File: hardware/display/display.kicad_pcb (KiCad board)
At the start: 2 copper layers, 110 x 70 mm, 7 parts, among them J1 Conn_02x03_Odd_Even

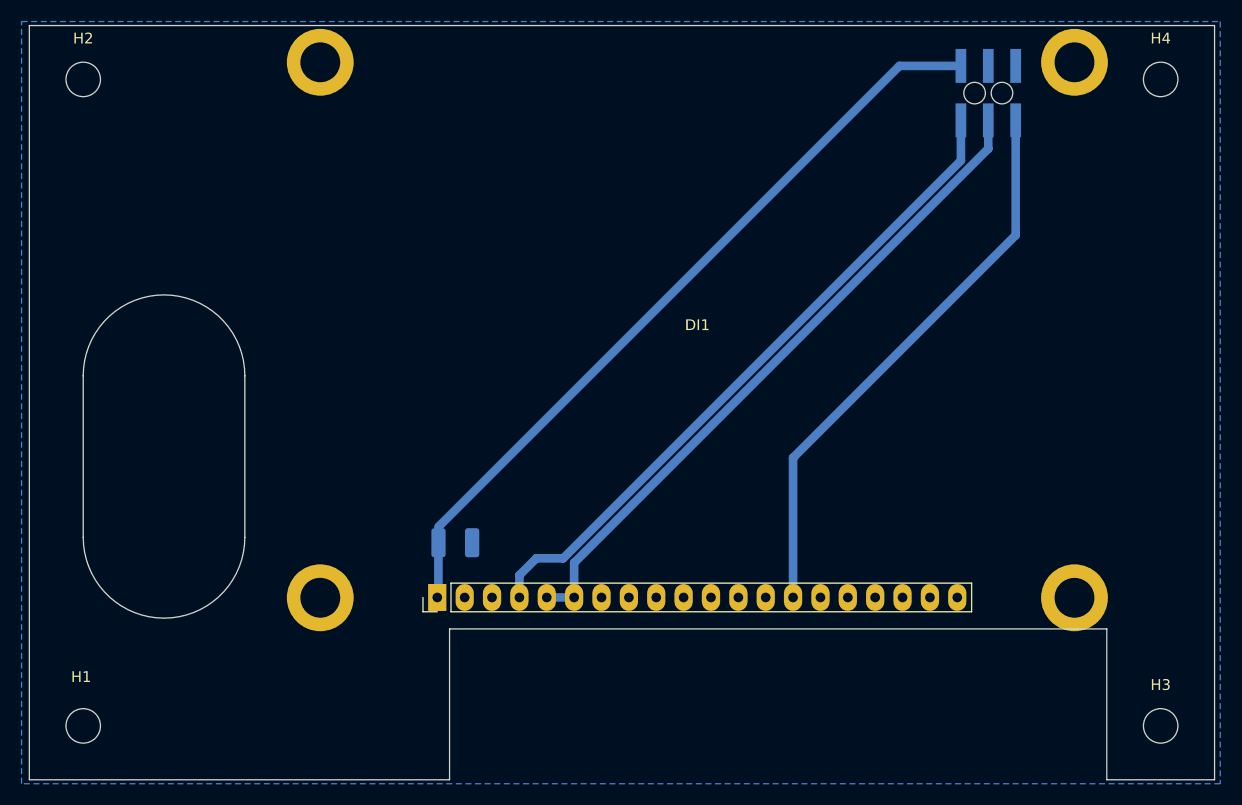
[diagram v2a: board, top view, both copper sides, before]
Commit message: Connect mounting holes to GND
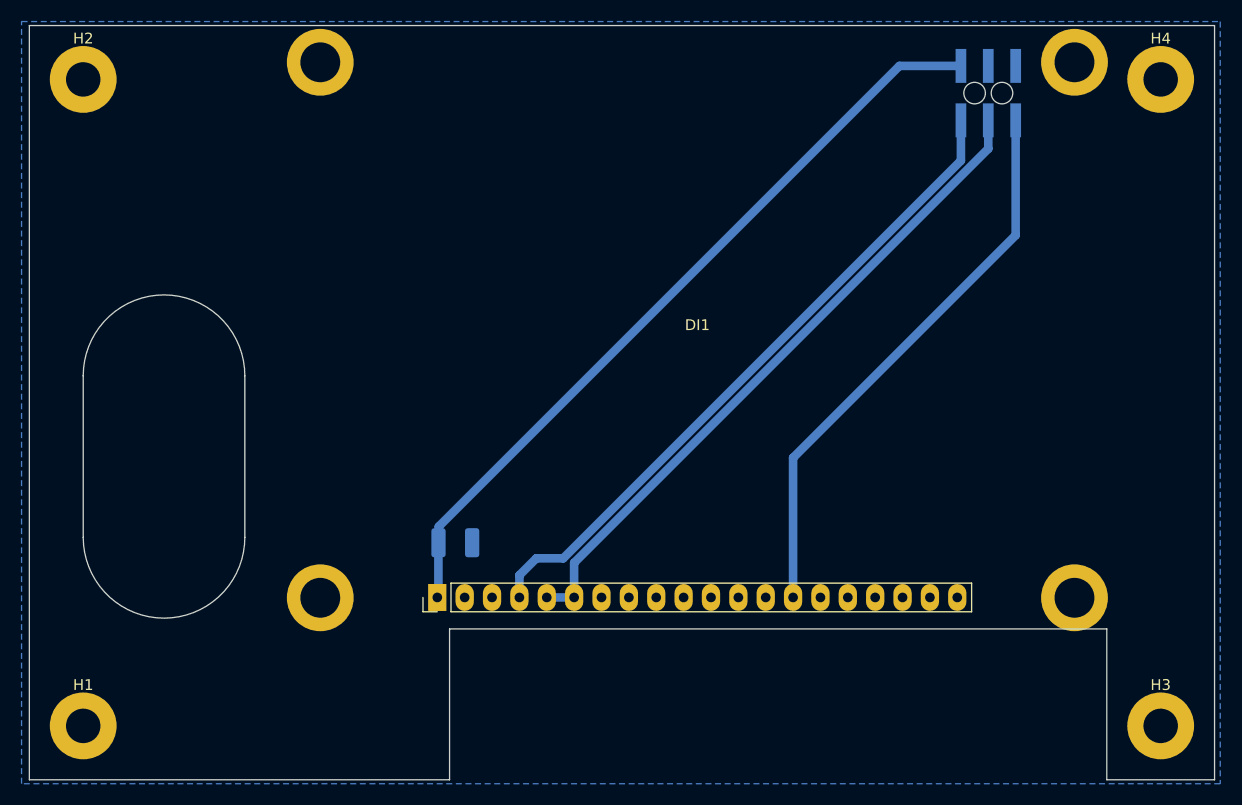
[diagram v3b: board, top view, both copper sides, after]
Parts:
- H1: footprint MountingHole:MountingHole_3.2mm_M3_DIN965 -> MountingHole:MountingHole_3.2mm_M3_DIN965_Pad
- H2, H3, H4: value 3.2mm -> MountingHole_Pad; footprint MountingHole:MountingHole_3.2mm_M3_DIN965 -> MountingHole:MountingHole_3.2mm_M3_DIN965_Pad
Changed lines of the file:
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@@
   (net 10 "/~{RST_DISP}")
   (net 11 "unconnected-(J1-Pad2)")
-  (footprint "MountingHole:MountingHole_3.2mm_M3_DIN965" locked (layer "F.Cu")
+  (footprint "MountingHole:MountingHole_3.2mm_M3_DIN965_Pad" locked (layer "F.Cu")
     (at 155 145)
-    (descr "Mounting Hole 3.2mm, no annular, M3, DIN965")
-    (tags "mounting hole 3.2mm no annular m3 din965")
+    (descr "Mounting Hole 3.2mm, M3, DIN965")
+    (tags "mounting hole 3.2mm m3 din965")
     (property "Sheetfile" "display.kicad_sch")
     (property "Sheetname" "")
@@
       (effects (font (size 1 1) (thickness 0.15)))
     )
-    (fp_text value "3.2mm" (at 0 3.8) (layer "F.Fab")
-      (effects (font (size 1 1) (thickness 0.15)))
-    )
-    (fp_text user "${REFERENCE}" (at 0 0) (layer "F.Fab")
-      (effects (font (size 1 1) (thickness 0.15)))
-    )
-    (fp_circle (center 0 0) (end 2.8 0) (layer "Cmts.User") (width 0.15) (fill none))
-    (fp_circle (center 0 0) (end 3.05 0) (layer "F.CrtYd") (width 0.05) (fill none))
-    (pad "" np_thru_hole circle locked (at 0 0) (size 3.2 3.2) (drill 3.2) (layers *.Cu *.Mask))
+    (fp_text value "MountingHole_Pad" (at 0 3.8) (layer "F.Fab")
+      (effects (font (size 1 1) (thickness 0.15)))
+    )
+    (fp_text user "${REFERENCE}" (at 0 0) (layer "F.Fab")
+      (effects (font (size 1 1) (thickness 0.15)))
+    )
+    (fp_circle (center 0 0) (end 2.8 0) (layer "Cmts.User") (width 0.15) (fill none))
+    (fp_circle (center 0 0) (end 3.05 0) (layer "F.CrtYd") (width 0.05) (fill none))
+    (pad "1" thru_hole circle locked (at 0 0) (size 6.2 6.2) (drill 3.2) (layers *.Cu *.Mask)
+      (net 1 "GND") (pinfunction "1") (pintype "input"))
   )
   (footprint "LCDdisplays.mod:MCOB128064JX" (layer "F.Cu")
@@
     )
   )
-  (footprint "MountingHole:MountingHole_3.2mm_M3_DIN965" locked (layer "F.Cu")
+  (footprint "MountingHole:MountingHole_3.2mm_M3_DIN965_Pad" locked (layer "F.Cu")
     (at 55 85)
-    (descr "Mounting Hole 3.2mm, no annular, M3, DIN965")
-    (tags "mounting hole 3.2mm no annular m3 din965")
+    (descr "Mounting Hole 3.2mm, M3, DIN965")
+    (tags "mounting hole 3.2mm m3 din965")
     (property "Sheetfile" "display.kicad_sch")
     (property "Sheetname" "")
@@
       (effects (font (size 1 1) (thickness 0.15)))
     )
+    (fp_text value "MountingHole_Pad" (at 0 3.8) (layer "F.Fab")
+      (effects (font (size 1 1) (thickness 0.15)))
+    )
+    (fp_text user "${REFERENCE}" (at 0 0) (layer "F.Fab")
+      (effects (font (size 1 1) (thickness 0.15)))
+    )
+    (fp_circle (center 0 0) (end 2.8 0) (layer "Cmts.User") (width 0.15) (fill none))
+    (fp_circle (center 0 0) (end 3.05 0) (layer "F.CrtYd") (width 0.05) (fill none))
+    (pad "1" thru_hole circle locked (at 0 0) (size 6.2 6.2) (drill 3.2) (layers *.Cu *.Mask)
+      (net 1 "GND") (pinfunction "1") (pintype "input"))
+  )
+  (footprint "MountingHole:MountingHole_3.2mm_M3_DIN965_Pad" locked (layer "F.Cu")
+    (at 55 145)
+    (descr "Mounting Hole 3.2mm, M3, DIN965")
+    (tags "mounting hole 3.2mm m3 din965")
+    (property "Sheetfile" "display.kicad_sch")
+    (property "Sheetname" "")
+    (attr exclude_from_pos_files)
+    (fp_text reference "H1" (at 0 -3.8) (layer "F.SilkS")
+      (effects (font (size 1 1) (thickness 0.15)))
+    )
     (fp_text value "3.2mm" (at 0 3.8) (layer "F.Fab")
       (effects (font (size 1 1) (thickness 0.15)))
@@
     (fp_circle (center 0 0) (end 2.8 0) (layer "Cmts.User") (width 0.15) (fill none))
     (fp_circle (center 0 0) (end 3.05 0) (layer "F.CrtYd") (width 0.05) (fill none))
-    (pad "" np_thru_hole circle locked (at 0 0) (size 3.2 3.2) (drill 3.2) (layers *.Cu *.Mask))
-  )
-  (footprint "MountingHole:MountingHole_3.2mm_M3_DIN965" locked (layer "F.Cu")
-    (at 55 145)
-    (descr "Mounting Hole 3.2mm, no annular, M3, DIN965")
-    (tags "mounting hole 3.2mm no annular m3 din965")
-    (property "Sheetfile" "display.kicad_sch")
-    (property "Sheetname" "")
-    (attr exclude_from_pos_files)
-    (fp_text reference "H1" (at -0.188 -4.538) (layer "F.SilkS")
-      (effects (font (size 1 1) (thickness 0.15)))
-    )
-    (fp_text value "3.2mm" (at 0 3.8) (layer "F.Fab")
-      (effects (font (size 1 1) (thickness 0.15)))
-    )
-    (fp_text user "${REFERENCE}" (at 0 0) (layer "F.Fab")
-      (effects (font (size 1 1) (thickness 0.15)))
-    )
-    (fp_circle (center 0 0) (end 2.8 0) (layer "Cmts.User") (width 0.15) (fill none))
-    (fp_circle (center 0 0) (end 3.05 0) (layer "F.CrtYd") (width 0.05) (fill none))
-    (pad "" np_thru_hole circle locked (at 0 0) (size 3.2 3.2) (drill 3.2) (layers *.Cu *.Mask))
-  )
-  (footprint "MountingHole:MountingHole_3.2mm_M3_DIN965" locked (layer "F.Cu")
+    (pad "1" thru_hole circle locked (at 0 0) (size 6.2 6.2) (drill 3.2) (layers *.Cu *.Mask)
+      (net 1 "GND") (pinfunction "1") (pintype "input"))
+  )
+  (footprint "MountingHole:MountingHole_3.2mm_M3_DIN965_Pad" locked (layer "F.Cu")
     (at 155 85)
-    (descr "Mounting Hole 3.2mm, no annular, M3, DIN965")
-    (tags "mounting hole 3.2mm no annular m3 din965")
+    (descr "Mounting Hole 3.2mm, M3, DIN965")
+    (tags "mounting hole 3.2mm m3 din965")
     (property "Sheetfile" "display.kicad_sch")
     (property "Sheetname" "")
@@
       (effects (font (size 1 1) (thickness 0.15)))
     )
-    (fp_text value "3.2mm" (at 0 3.8) (layer "F.Fab")
-      (effects (font (size 1 1) (thickness 0.15)))
-    )
-    (fp_text user "${REFERENCE}" (at 0 0) (layer "F.Fab")
-      (effects (font (size 1 1) (thickness 0.15)))
-    )
-    (fp_circle (center 0 0) (end 2.8 0) (layer "Cmts.User") (width 0.15) (fill none))
-    (fp_circle (center 0 0) (end 3.05 0) (layer "F.CrtYd") (width 0.05) (fill none))
-    (pad "" np_thru_hole circle locked (at 0 0) (size 3.2 3.2) (drill 3.2) (layers *.Cu *.Mask))
+    (fp_text value "MountingHole_Pad" (at 0 3.8) (layer "F.Fab")
+      (effects (font (size 1 1) (thickness 0.15)))
+    )
+    (fp_text user "${REFERENCE}" (at 0 0) (layer "F.Fab")
+      (effects (font (size 1 1) (thickness 0.15)))
+    )
+    (fp_circle (center 0 0) (end 2.8 0) (layer "Cmts.User") (width 0.15) (fill none))
+    (fp_circle (center 0 0) (end 3.05 0) (layer "F.CrtYd") (width 0.05) (fill none))
+    (pad "1" thru_hole circle locked (at 0 0) (size 6.2 6.2) (drill 3.2) (layers *.Cu *.Mask)
+      (net 1 "GND") (pinfunction "1") (pintype "input"))
   )
   (footprint "harwin:M20-8750342" locked (layer "B.Cu")

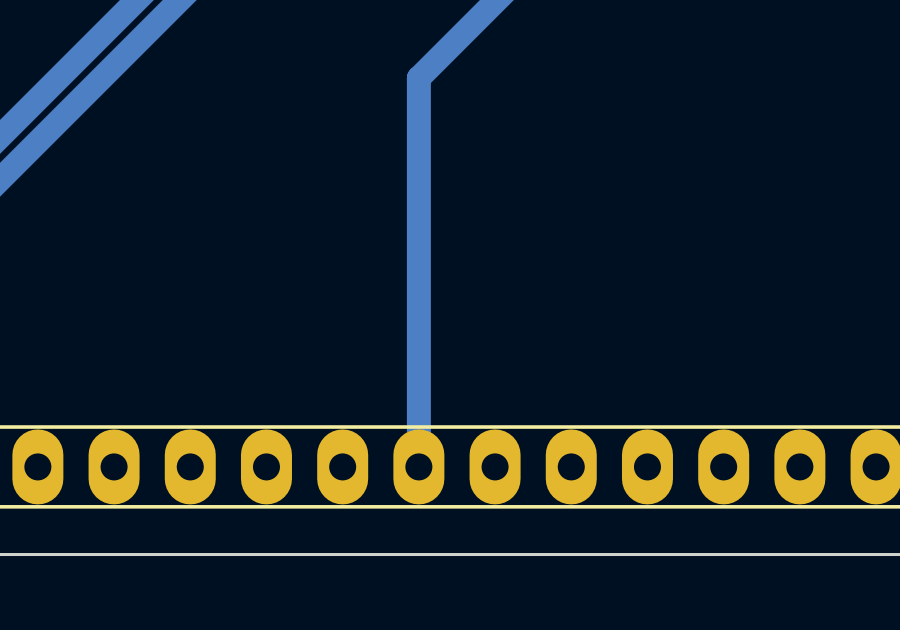
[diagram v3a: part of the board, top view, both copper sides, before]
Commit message: Add a pulldown resistor to /RST_DISP
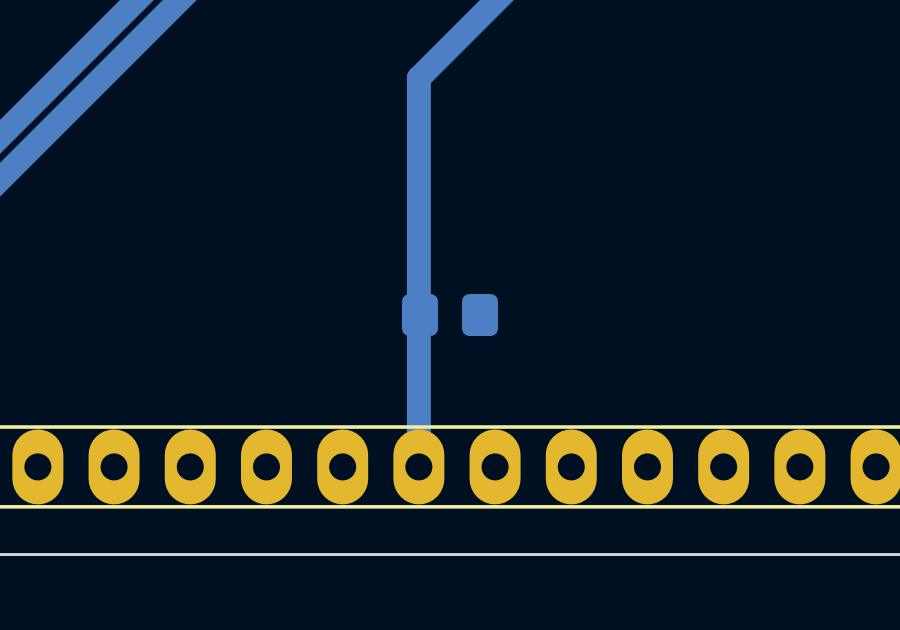
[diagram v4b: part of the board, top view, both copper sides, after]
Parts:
- added R1: 10k, Resistor_SMD:R_0805_2012Metric_Pad1.20x1.40mm_HandSolder, B.Cu at (121.9, 128.0)
- H2, H3, H4: value MountingHole_Pad -> 3.2mm
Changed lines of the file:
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@@
     (descr "Mounting Hole 3.2mm, M3, DIN965")
     (tags "mounting hole 3.2mm m3 din965")
+    (property "P/N" "N/A")
     (property "Sheetfile" "display.kicad_sch")
     (property "Sheetname" "")
@@
       (effects (font (size 1 1) (thickness 0.15)))
     )
-    (fp_text value "MountingHole_Pad" (at 0 3.8) (layer "F.Fab")
+    (fp_text value "3.2mm" (at 0 3.8) (layer "F.Fab")
       (effects (font (size 1 1) (thickness 0.15)))
     )
@@
   (footprint "LCDdisplays.mod:MCOB128064JX" (layer "F.Cu")
     (at 112 105)
-    (property "P/N" "MCOB128064JX-YM")
+    (property "P/N" "MCOB128064JX-YM (F)")
     (property "Sheetfile" "display.kicad_sch")
     (property "Sheetname" "")
@@
     (descr "Mounting Hole 3.2mm, M3, DIN965")
     (tags "mounting hole 3.2mm m3 din965")
+    (property "P/N" "N/A")
     (property "Sheetfile" "display.kicad_sch")
     (property "Sheetname" "")
@@
       (effects (font (size 1 1) (thickness 0.15)))
     )
-    (fp_text value "MountingHole_Pad" (at 0 3.8) (layer "F.Fab")
+    (fp_text value "3.2mm" (at 0 3.8) (layer "F.Fab")
       (effects (font (size 1 1) (thickness 0.15)))
     )
@@
     (descr "Mounting Hole 3.2mm, M3, DIN965")
     (tags "mounting hole 3.2mm m3 din965")
+    (property "P/N" "N/A")
     (property "Sheetfile" "display.kicad_sch")
     (property "Sheetname" "")
@@
     (descr "Mounting Hole 3.2mm, M3, DIN965")
     (tags "mounting hole 3.2mm m3 din965")
+    (property "P/N" "N/A")
     (property "Sheetfile" "display.kicad_sch")
     (property "Sheetname" "")
@@
       (effects (font (size 1 1) (thickness 0.15)))
     )
-    (fp_text value "MountingHole_Pad" (at 0 3.8) (layer "F.Fab")
-      (effects (font (size 1 1) (thickness 0.15)))
-    )
-    (fp_text user "${REFERENCE}" (at 0 0) (layer "F.Fab")
-      (effects (font (size 1 1) (thickness 0.15)))
-    )
-    (fp_circle (center 0 0) (end 2.8 0) (layer "Cmts.User") (width 0.15) (fill none))
-    (fp_circle (center 0 0) (end 3.05 0) (layer "F.CrtYd") (width 0.05) (fill none))
-    (pad "1" thru_hole circle locked (at 0 0) (size 6.2 6.2) (drill 3.2) (layers *.Cu *.Mask)
-      (net 1 "GND") (pinfunction "1") (pintype "input"))
+    (fp_text value "3.2mm" (at 0 3.8) (layer "F.Fab")
+      (effects (font (size 1 1) (thickness 0.15)))
+    )
+    (fp_text user "${REFERENCE}" (at 0 0) (layer "F.Fab")
+      (effects (font (size 1 1) (thickness 0.15)))
+    )
+    (fp_circle (center 0 0) (end 2.8 0) (layer "Cmts.User") (width 0.15) (fill none))
+    (fp_circle (center 0 0) (end 3.05 0) (layer "F.CrtYd") (width 0.05) (fill none))
+    (pad "1" thru_hole circle locked (at 0 0) (size 6.2 6.2) (drill 3.2) (layers *.Cu *.Mask)
+      (net 1 "GND") (pinfunction "1") (pintype "input"))
+  )
+  (footprint "Resistor_SMD:R_0805_2012Metric_Pad1.20x1.40mm_HandSolder" (layer "B.Cu")
+    (at 121.92 128.016)
+    (descr "Resistor SMD 0805 (2012 Metric), square (rectangular) end terminal, IPC_7351 nominal with elongated pad for handsoldering. (Body size source: IPC-SM-782 page 72, https://www.pcb-3d.com/wordpress/wp-content/uploads/ipc-sm-782a_amendment_1_and_2.pdf), generated with kicad-footprint-generator")
+    (tags "resistor handsolder")
+    (property "P/N" "Stock")
+    (property "Sheetfile" "display.kicad_sch")
+    (property "Sheetname" "")
+    (attr smd)
+    (fp_text reference "R1" (at 0 1.65) (layer "B.SilkS")
+      (effects (font (size 1 1) (thickness 0.15)) (justify mirror))
+    )
+    (fp_text value "10k" (at 0 -1.65) (layer "B.Fab")
+      (effects (font (size 1 1) (thickness 0.15)) (justify mirror))
+    )
+    (fp_text user "${REFERENCE}" (at 0 0) (layer "B.Fab")
+      (effects (font (size 0.5 0.5) (thickness 0.08)) (justify mirror))
+    )
+    (fp_line (start -0.227064 0.735) (end 0.227064 0.735) (layer "B.SilkS") (width 0.12))
+    (fp_line (start -0.227064 -0.735) (end 0.227064 -0.735) (layer "B.SilkS") (width 0.12))
+    (fp_line (start 1.85 -0.95) (end -1.85 -0.95) (layer "B.CrtYd") (width 0.05))
+    (fp_line (start 1.85 0.95) (end 1.85 -0.95) (layer "B.CrtYd") (width 0.05))
+    (fp_line (start -1.85 -0.95) (end -1.85 0.95) (layer "B.CrtYd") (width 0.05))
+    (fp_line (start -1.85 0.95) (end 1.85 0.95) (layer "B.CrtYd") (width 0.05))
+    (fp_line (start 1 0.625) (end 1 -0.625) (layer "B.Fab") (width 0.1))
+    (fp_line (start -1 -0.625) (end -1 0.625) (layer "B.Fab") (width 0.1))
+    (fp_line (start 1 -0.625) (end -1 -0.625) (layer "B.Fab") (width 0.1))
+    (fp_line (start -1 0.625) (end 1 0.625) (layer "B.Fab") (width 0.1))
+    (pad "1" smd roundrect (at -1 0) (size 1.2 1.4) (layers "B.Cu" "B.Paste" "B.Mask") (roundrect_rratio 0.208333)
+      (net 10 "/~{RST_DISP}") (pintype "passive"))
+    (pad "2" smd roundrect (at 1 0) (size 1.2 1.4) (layers "B.Cu" "B.Paste" "B.Mask") (roundrect_rratio 0.208333)
+      (net 1 "GND") (pintype "passive"))
+    (model "${KICAD6_3DMODEL_DIR}/Resistor_SMD.3dshapes/R_0805_2012Metric.wrl"
+      (offset (xyz 0 0 0))
+      (scale (xyz 1 1 1))
+      (rotate (xyz 0 0 0))
+    )
   )
   (footprint "harwin:M20-8750342" locked (layer "B.Cu")
     (at 139 86.27 -90)
-    (property "P/N" " M20-8750342 ")
-    (property "Sheetfile" "display.kicad_sch")
-    (property "Sheetname" "")
+    (property "P/N" "M20-8750342 (M)")
+    (property "Sheetfile" "display.kicad_sch")
+    (property "Sheetname" "")
